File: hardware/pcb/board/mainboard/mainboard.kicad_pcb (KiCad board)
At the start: 6 copper layers, 76.4 x 55 mm, 136 parts, among them J1 Conn_Coaxial, J10 USB_C_Receptacle, J11 2908-05WB-MG, J2 USB_C_Receptacle_USB2.0_16P, J3 Conn_02x35_Odd_Even_MountingP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, J4 Conn_02x40_Odd_Even_MountingP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, J5 Conn_02x40_Odd_Even_MountingP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, J7 Conn_01x30, J8 Conn_01x30, J9 Conn_01x30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

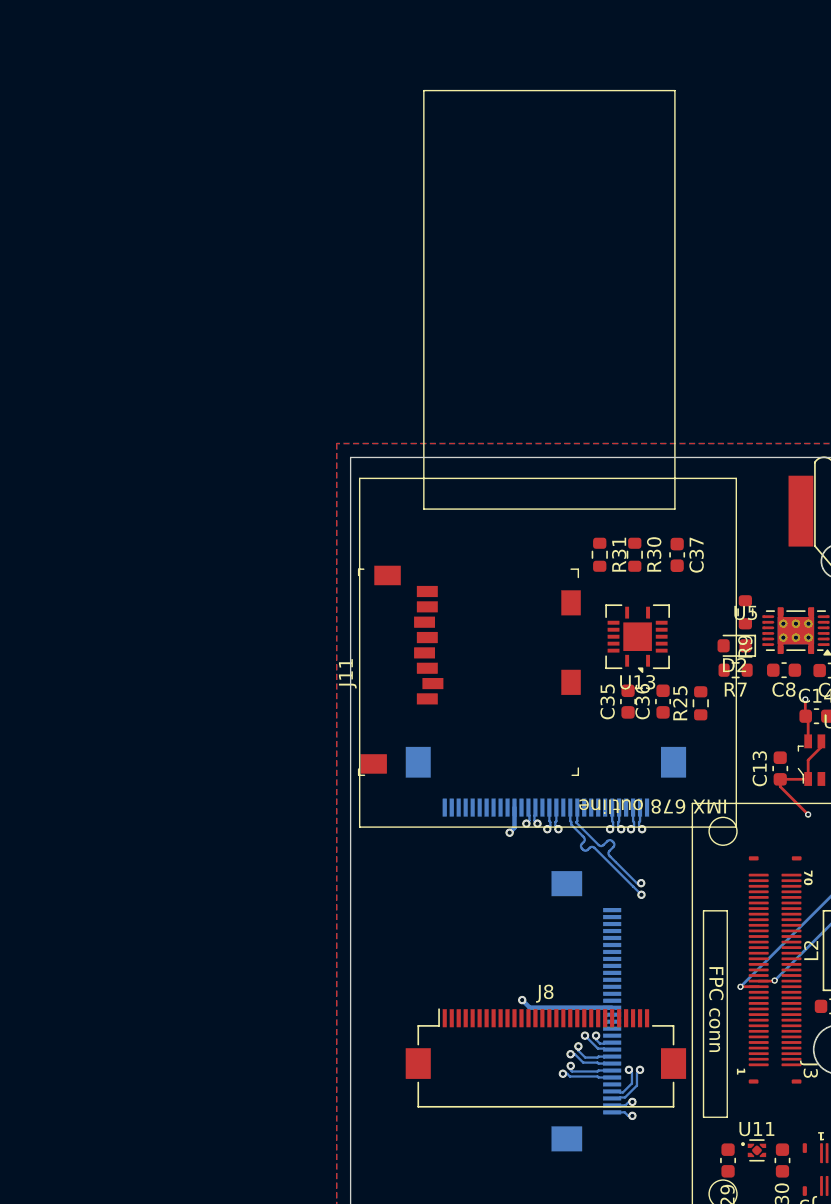
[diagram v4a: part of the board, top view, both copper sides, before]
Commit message: new 3V3 setup for cameras, 30 pin mipi connections
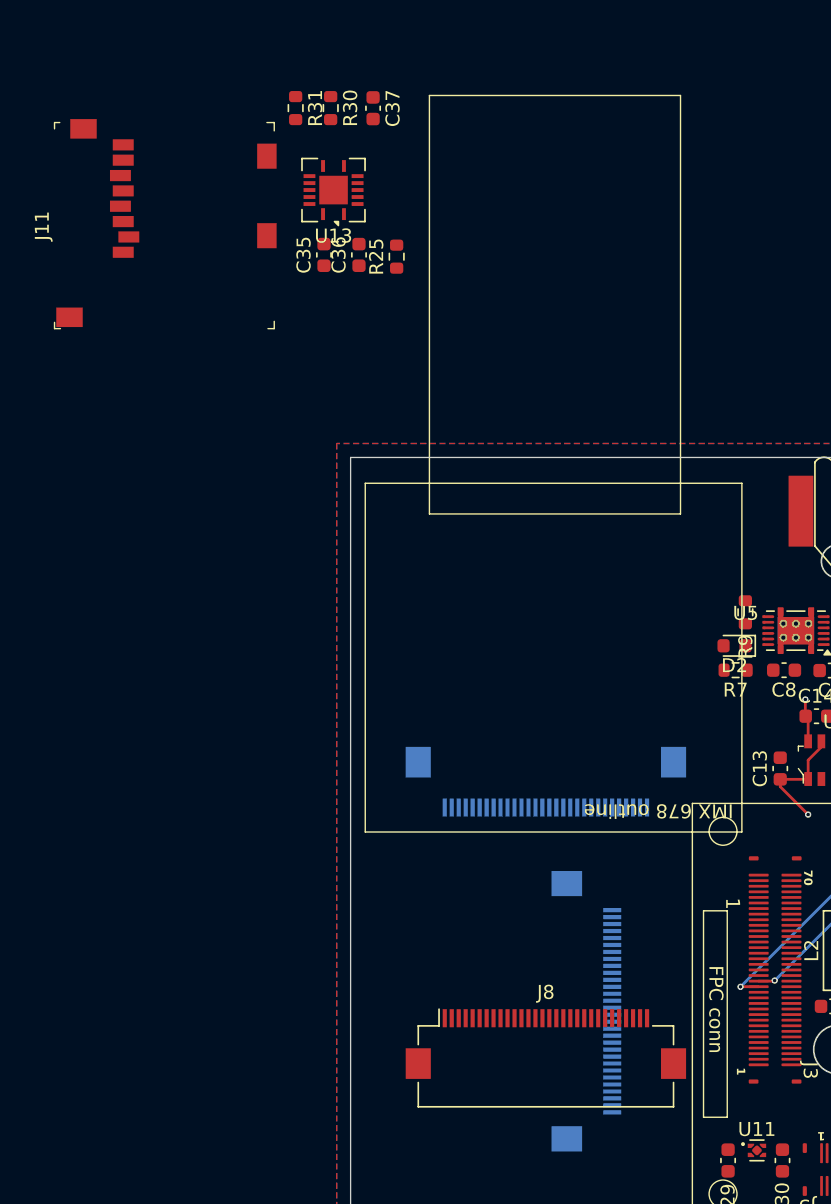
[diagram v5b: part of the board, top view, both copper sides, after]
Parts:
- moved C36 38.7 mm to (100.6, 85.5)
- moved R30 38.7 mm to (98.6, 75.0)
- moved C35 38.7 mm to (98.1, 85.5)
- moved C37 38.7 mm to (101.6, 75.0)
- moved J11 38.7 mm to (83.7, 85.3)
- moved R25 38.7 mm to (103.3, 85.6)
- moved R31 38.7 mm to (96.1, 75.0)
- moved U13 38.7 mm to (98.8, 80.8)
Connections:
- net CSI1_CKN renamed CSI0_CKN
- net CSI1_CKP renamed CSI0_CKP
- net CSI1_DN0 renamed CSI0_DN0
- net CSI1_DN1 renamed CSI0_DN1
- net CSI1_DN2 renamed CSI0_DN2
- net CSI1_DN3 renamed CSI0_DN3
- net CSI1_DP0 renamed CSI0_DP0
- net CSI1_DP1 renamed CSI0_DP1
- net CSI1_DP2 renamed CSI0_DP2
- net CSI1_DP3 renamed CSI0_DP3
- net H_GPIO_14 renamed H_GPIO_17
- net H_GPIO_9 renamed H_GPIO_16
- net H_SPI_CSI renamed H_SPI_CS1
- net LINK_ST/PHY_CRG1 renamed LINK_ST/PHY_CFG1
- J3 pad 18: unconnected-(J3-Pin_18-Pad18) -> CSI_1_CKP
- J3 pad 20: unconnected-(J3-Pin_20-Pad20) -> CSI_1_CKN
- J3 pad 28: H_GPIO_25 -> H_GPIO_27
- J3 pad 3: BOOT MODE -> H_I2S_SDO
- J3 pad 32: unconnected-(J3-Pin_32-Pad32) -> CSI_1_DN2
- J3 pad 34: unconnected-(J3-Pin_34-Pad34) -> CSI_1_DP2
- J3 pad 38: unconnected-(J3-Pin_38-Pad38) -> CSI_1_DN3
- J3 pad 40: unconnected-(J3-Pin_40-Pad40) -> CSI_1_DP3
- J3 pad 49: unconnected-(J3-Pin_49-Pad49) -> CSI_1_DN1
- J3 pad 51: unconnected-(J3-Pin_51-Pad51) -> CSI_1_DP1
- J3 pad 53: unconnected-(J3-Pin_53-Pad53) -> CSI_1_DN0
- J3 pad 55: unconnected-(J3-Pin_55-Pad55) -> CSI_1_DP0
- J5 pad 10: H_GPIO_27 -> H_GPIO_25
- J5 pad 24: GPIO1_4 -> GPIO0_4
- J5 pad 28: unconnected-(J5-Pin_28-Pad28) -> H_GPIO_3
- J5 pad 70: unconnected-(J5-Pin_70-Pad70) -> GND
- J7 pad 1: 3V3 -> unconnected-(J7-Pin_1-Pad1)
- J7 pad 11: CAM0_MClk -> unconnected-(J7-Pin_11-Pad11)
- J7 pad 13: CAM0_MCP -> unconnected-(J7-Pin_13-Pad13)
- J7 pad 14: CAM0_MCN -> unconnected-(J7-Pin_14-Pad14)
- J7 pad 15: GND -> unconnected-(J7-Pin_15-Pad15)
- J7 pad 16: CAM0_MDP0 -> unconnected-(J7-Pin_16-Pad16)
- J7 pad 17: CAM0_MDN0 -> unconnected-(J7-Pin_17-Pad17)
- J7 pad 18: GND -> unconnected-(J7-Pin_18-Pad18)
- J7 pad 19: CAM0_MDP1 -> unconnected-(J7-Pin_19-Pad19)
- J7 pad 2: 3V3 -> unconnected-(J7-Pin_2-Pad2)
- J7 pad 20: CAM0_MDN1 -> unconnected-(J7-Pin_20-Pad20)
- J7 pad 21: GND -> unconnected-(J7-Pin_21-Pad21)
- J7 pad 24: GND -> unconnected-(J7-Pin_24-Pad24)
- J7 pad 25: CAM0_MDP2 -> unconnected-(J7-Pin_25-Pad25)
- J7 pad 26: CAM0_MDN2 -> unconnected-(J7-Pin_26-Pad26)
- J7 pad 27: GND -> unconnected-(J7-Pin_27-Pad27)
- J7 pad 28: CAM0_MDP3 -> unconnected-(J7-Pin_28-Pad28)
- J7 pad 29: CAM0_MDN3 -> unconnected-(J7-Pin_29-Pad29)
- J7 pad 3: 3V3 -> unconnected-(J7-Pin_3-Pad3)
- J7 pad 30: GND -> unconnected-(J7-Pin_30-Pad30)
- J7 pad 4: GND -> unconnected-(J7-Pin_4-Pad4)
- J7 pad 5: GND -> unconnected-(J7-Pin_5-Pad5)
- J7 pad 6: D0VDD -> unconnected-(J7-Pin_6-Pad6)
- J7 pad 7: CAM0_RESET -> unconnected-(J7-Pin_7-Pad7)
- J7 pad 8: I2C0_SDA -> unconnected-(J7-Pin_8-Pad8)
- J7 pad 9: I2C0_SCL -> unconnected-(J7-Pin_9-Pad9)
- J8 pad 1: 3V3 -> GND
- J8 pad 10: unconnected-(J8-Pin_10-Pad10) -> GND
- J8 pad 11: CAM1_MClk -> CAM1_MDN1
- J8 pad 12: unconnected-(J8-Pin_12-Pad12) -> CAM1_MDP1
- J8 pad 13: CAM1_MCP -> GND
- J8 pad 14: CAM1_MCN -> CAM1_MDN0
- J8 pad 15: GND -> CAM1_MDP0
- J8 pad 16: CAM1_MDP0 -> GND
- J8 pad 17: CAM1_MDN0 -> CAM1_MCN
- J8 pad 18: GND -> CAM1_MCP
- J8 pad 19: CAM1_MDP1 -> unconnected-(J8-Pin_19-Pad19)
- J8 pad 2: 3V3 -> CAM1_MDN3
- J8 pad 20: CAM1_MDN1 -> CAM1_MClk
- J8 pad 21: GND -> unconnected-(J8-Pin_21-Pad21)
- J8 pad 22: unconnected-(J8-Pin_22-Pad22) -> H_I2C2_SCL
- J8 pad 23: unconnected-(J8-Pin_23-Pad23) -> H_I2C2_SDA
- J8 pad 24: GND -> CAM1_RESET
- J8 pad 25: CAM1_MDP2 -> D0VDD
- J8 pad 26: CAM1_MDN2 -> GND
- J8 pad 28: CAM1_MDP3 -> 3V3
- J8 pad 29: CAM1_MDN3 -> 3V3
- J8 pad 3: 3V3 -> CAM1_MDP3
- J8 pad 30: GND -> 3V3
- J8 pad 5: GND -> CAM1_MDN2
- J8 pad 6: D0VDD -> CAM1_MDP2
- J8 pad 7: CAM1_RESET -> GND
- J8 pad 8: H_I2C2_SDA -> unconnected-(J8-Pin_8-Pad8)
- J8 pad 9: H_I2C2_SCL -> unconnected-(J8-Pin_9-Pad9)
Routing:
- net CAM0_MClk: track 25.4 -> 0.00 mm, vias 2 -> 0
- net CAM0_MDP3: track 25.4 -> 0.00 mm, vias 2 -> 0
- net CAM0_MDN1: track 25.4 -> 0.00 mm, vias 2 -> 0
- net CAM0_MDP1: track 25.4 -> 0.00 mm, vias 2 -> 0
- net CAM0_MCP: track 25.4 -> 0.00 mm, vias 2 -> 0
- net CAM0_MDN3: track 25.4 -> 0.00 mm, vias 2 -> 0
- net CAM0_MCN: track 25.3 -> 0.00 mm, vias 2 -> 0
- net CAM0_MDP2: track 25.3 -> 0.00 mm, vias 2 -> 0
- net CAM0_MDN0: track 25.3 -> 0.00 mm, vias 2 -> 0
- net CAM0_MDN2: track 25.3 -> 0.00 mm, vias 2 -> 0
- net CAM0_MDP0: track 25.3 -> 0.00 mm, vias 2 -> 0
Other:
- board text added: "1"

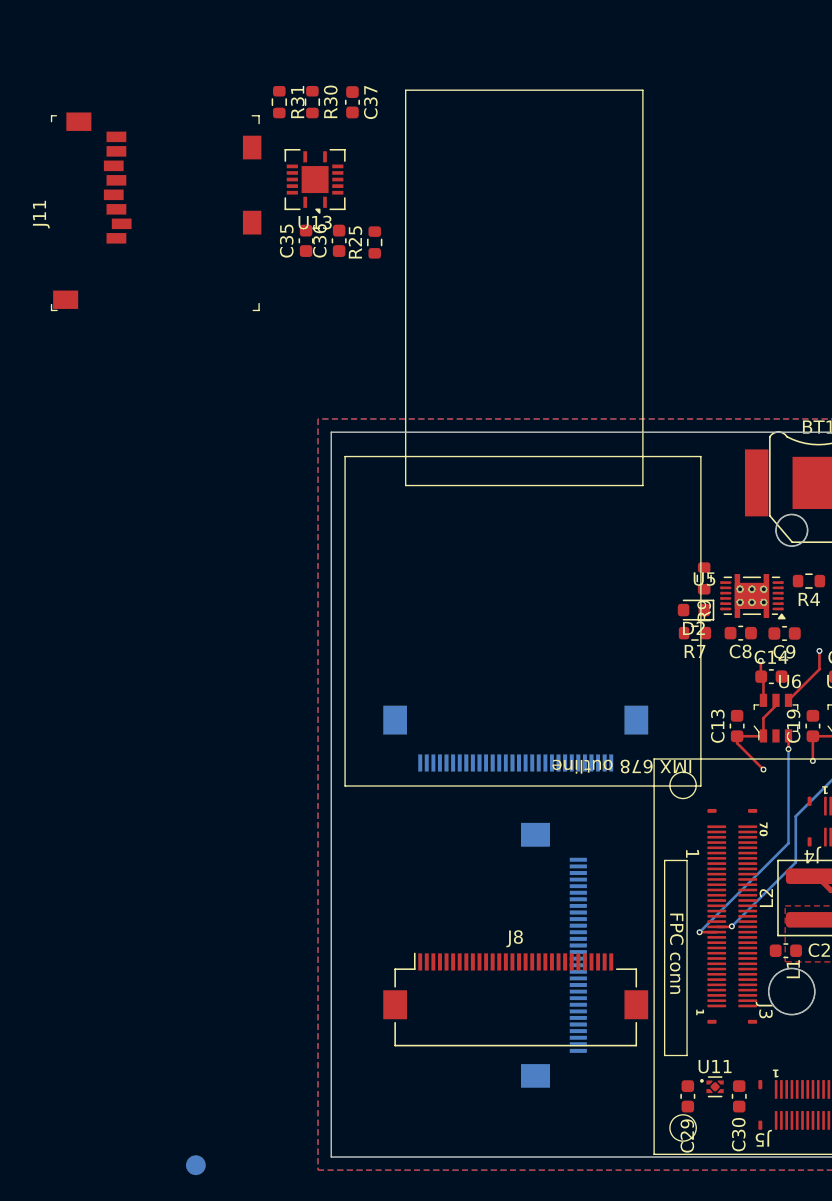
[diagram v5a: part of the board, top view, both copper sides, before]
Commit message: place ment of new 3V3 + oscillators + reset mechanic
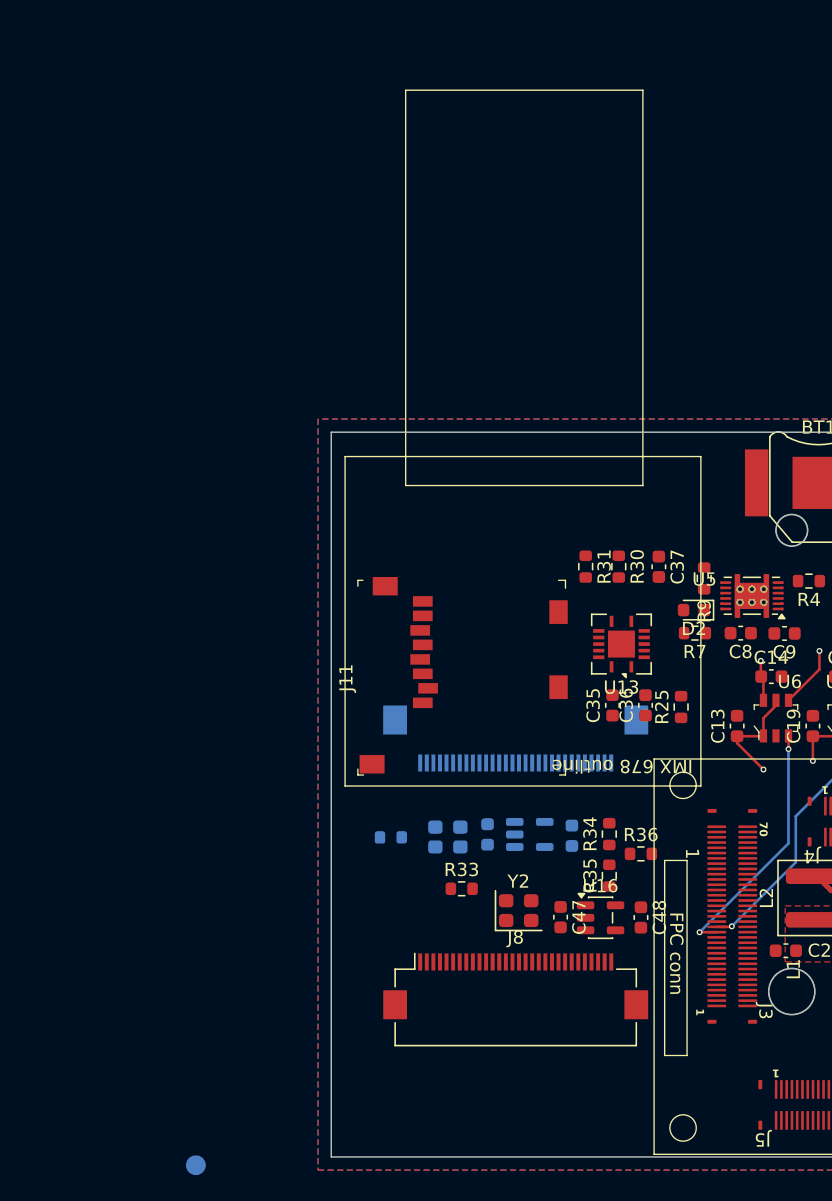
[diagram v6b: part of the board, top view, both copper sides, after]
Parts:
- removed C29, C30: 1 uF, Capacitor_SMD:C_0603_1608Metric
- removed J9: Conn_01x30, Connector_FFC-FPC:Hirose_FH12-30S-0.5SH_1x30-1MP_P0.50mm_Horizontal
- removed U11: TPS7A20_SOT-23, Package_SON:Texas_X2SON-4_1x1mm_P0.65mm
- added C47: 1 uF, Capacitor_SMD:C_0603_1608Metric, F.Cu at (117.4, 136.8)
- added C48: 1 uf, Capacitor_SMD:C_0603_1608Metric, F.Cu at (123.5, 136.8)
- added C49: 1 uF, Capacitor_SMD:C_0603_1608Metric, B.Cu at (111.9, 130.5)
- added C50: 1 uf, Capacitor_SMD:C_0603_1608Metric, B.Cu at (118.3, 130.6)
- added R21: 0, Resistor_SMD:R_0603_1608Metric, B.Cu at (104.5, 130.7)
- added R33: 0, Resistor_SMD:R_0603_1608Metric, F.Cu at (109.9, 134.7)
- added R34: 10k, Resistor_SMD:R_0603_1608Metric, F.Cu at (121.1, 130.5)
- added R35: 10k, Resistor_SMD:R_0603_1608Metric, F.Cu at (121.1, 133.7)
- added R36: 0, Resistor_SMD:R_0603_1608Metric, F.Cu at (123.5, 132.0)
- added U16: TLV77733PDBVR, Package_TO_SOT_SMD:SOT-23-5, F.Cu at (120.4, 136.8)
- added U17: TLV77733PDBVR, Package_TO_SOT_SMD:SOT-23-5, B.Cu at (115.1, 130.5)
- added Y1: SiT8008xx-1x-xxE, Oscillator:Oscillator_SMD_SiT_PQFN-4Pin_2.5x2.0mm, B.Cu at (108.8, 130.7)
- added Y2: SiT8008xx-1x-xxE, Oscillator:Oscillator_SMD_SiT_PQFN-4Pin_2.5x2.0mm, F.Cu at (114.2, 136.3)
- moved C35 42.2 mm to (121.3, 120.7)
- moved C36 42.2 mm to (123.8, 120.7)
- moved C37 42.2 mm to (124.9, 110.2)
- moved J11 42.2 mm to (107.0, 120.5)
- moved R25 42.2 mm to (126.5, 120.9)
- moved R30 42.2 mm to (121.8, 110.2)
- moved R31 42.2 mm to (119.3, 110.2)
- moved U13 42.2 mm to (122.0, 116.1)
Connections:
- net 3V3 renamed CAM1_3V3
- J3 pad 46: H_GPIO_19 -> CAM0_RESET
- J4 pad 71: VDD_5V -> +5V
- J4 pad 73: VDD_5V -> +5V
- J4 pad 75: VDD_5V -> +5V
- J4 pad 77: VDD_5V -> +5V
- J4 pad 79: VDD_5V -> +5V
- J7 pad 1: unconnected-(J7-Pin_1-Pad1) -> GND
- J7 pad 10: unconnected-(J7-Pin_10-Pad10) -> GND
- J7 pad 11: unconnected-(J7-Pin_11-Pad11) -> CSI0_DN1
- J7 pad 12: unconnected-(J7-Pin_12-Pad12) -> CSI0_DP1
- J7 pad 13: unconnected-(J7-Pin_13-Pad13) -> GND
- J7 pad 14: unconnected-(J7-Pin_14-Pad14) -> CSI0_DN0
- J7 pad 15: unconnected-(J7-Pin_15-Pad15) -> CSI0_DP0
- J7 pad 16: unconnected-(J7-Pin_16-Pad16) -> GND
- J7 pad 17: unconnected-(J7-Pin_17-Pad17) -> CSI0_CKN
- J7 pad 18: unconnected-(J7-Pin_18-Pad18) -> CSI0_CKP
- J7 pad 2: unconnected-(J7-Pin_2-Pad2) -> CSI0_DN3
- J7 pad 20: unconnected-(J7-Pin_20-Pad20) -> CAM0_MClk
- J7 pad 22: unconnected-(J7-Pin_22-Pad22) -> I2C0_SCL
- J7 pad 23: unconnected-(J7-Pin_23-Pad23) -> I2C0_SDA
- J7 pad 24: unconnected-(J7-Pin_24-Pad24) -> Net-(J7-Pin_24)
- J7 pad 25: unconnected-(J7-Pin_25-Pad25) -> VDD_1V8
- J7 pad 26: unconnected-(J7-Pin_26-Pad26) -> GND
- J7 pad 27: unconnected-(J7-Pin_27-Pad27) -> GND
- J7 pad 28: unconnected-(J7-Pin_28-Pad28) -> CAM0_3V3
- J7 pad 29: unconnected-(J7-Pin_29-Pad29) -> CAM0_3V3
- J7 pad 3: unconnected-(J7-Pin_3-Pad3) -> CSI0_DP3
- J7 pad 30: unconnected-(J7-Pin_30-Pad30) -> CAM0_3V3
- J7 pad 4: unconnected-(J7-Pin_4-Pad4) -> GND
- J7 pad 5: unconnected-(J7-Pin_5-Pad5) -> CSI0_DN2
- J7 pad 6: unconnected-(J7-Pin_6-Pad6) -> CSI0_DP2
- J7 pad 7: unconnected-(J7-Pin_7-Pad7) -> GND
- J8 pad 11: CAM1_MDN1 -> CSI_1_DN1
- J8 pad 12: CAM1_MDP1 -> CSI_1_DP1
- J8 pad 14: CAM1_MDN0 -> CSI_1_DN0
- J8 pad 15: CAM1_MDP0 -> CSI_1_DP0
- J8 pad 17: CAM1_MCN -> CSI_1_CKN
- J8 pad 18: CAM1_MCP -> CSI_1_CKP
- J8 pad 2: CAM1_MDN3 -> CSI_1_DN3
- J8 pad 24: CAM1_RESET -> CAM0_RESET
- J8 pad 25: D0VDD -> VDD_1V8
- J8 pad 3: CAM1_MDP3 -> CSI_1_DP3
- J8 pad 5: CAM1_MDN2 -> CSI_1_DN2
- J8 pad 6: CAM1_MDP2 -> CSI_1_DP2
